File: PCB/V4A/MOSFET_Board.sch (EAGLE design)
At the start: 68 parts, among them IC101 7805T, Q101 IXTK102N65X2, Q102 BC817-16SMD, Q103 SIRC10DP, Q104 SIRC10DP, Q105 BC817-16SMD, Q106 BC807-16SMD, U101 AD620, U102 AD620, U103 LTC1865L, U104 LT1014I, U105 AD420, U106 LP2985-3.1, X201 SMKDSP_1,5/2, X202 SMKDSP_1,5/2

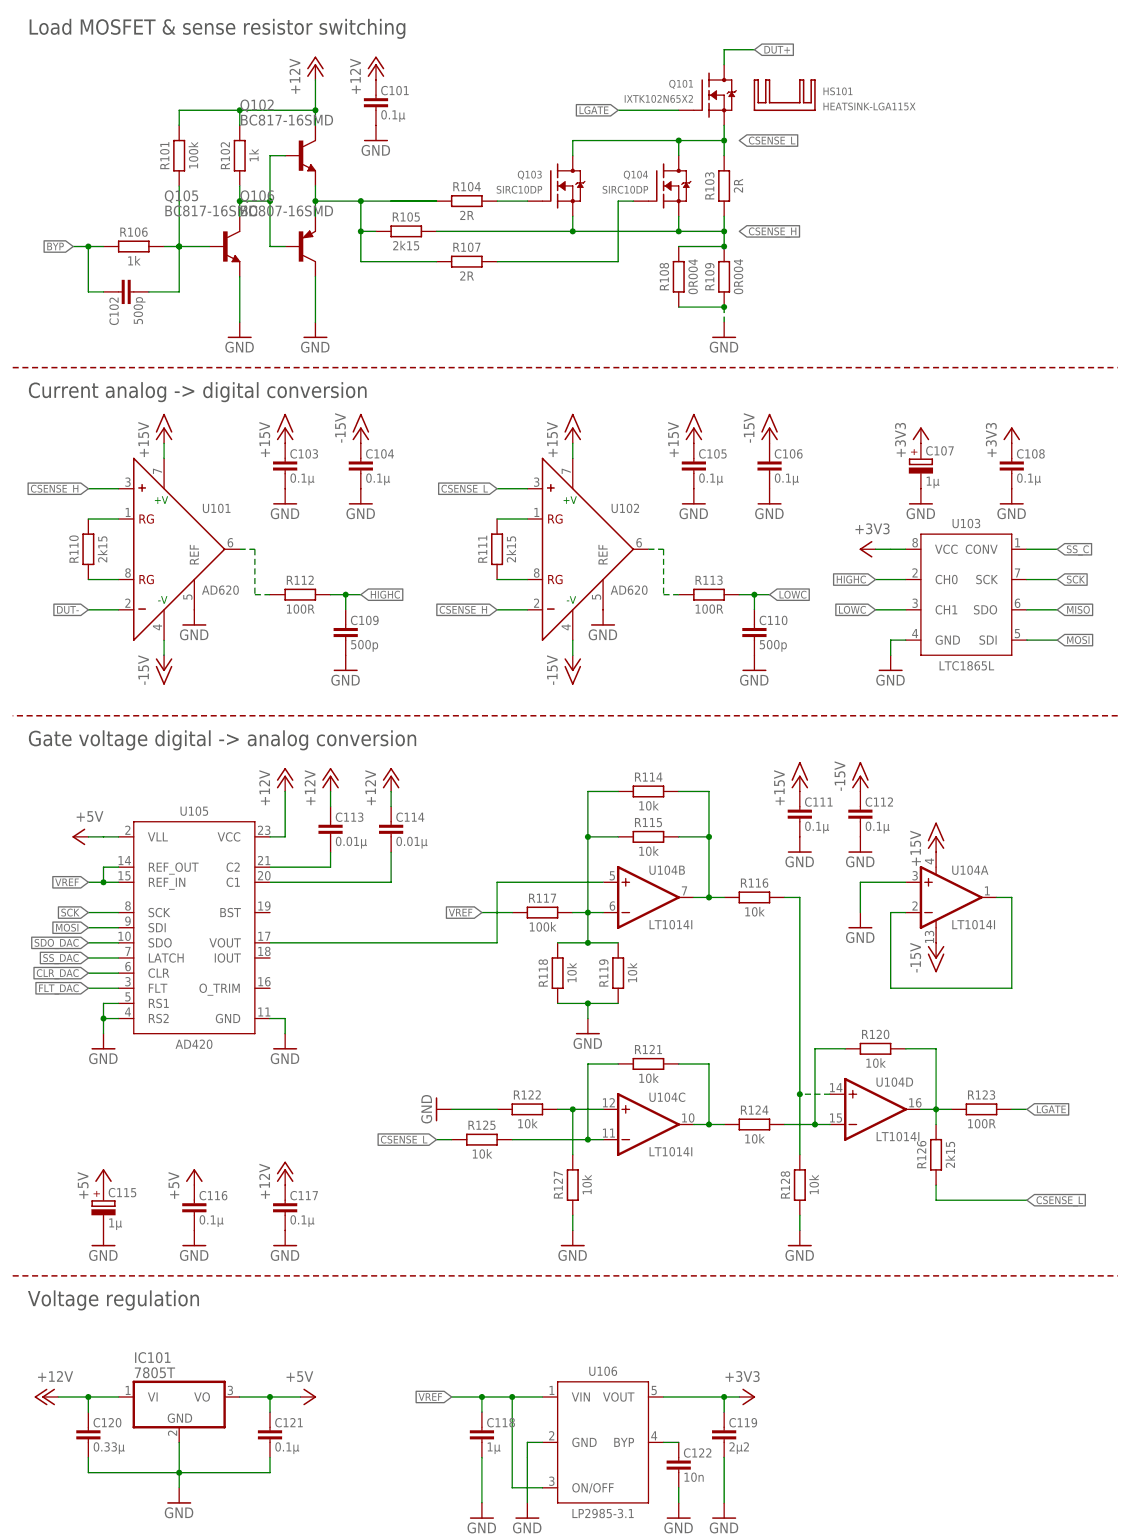
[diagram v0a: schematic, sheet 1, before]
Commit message: Added optoisolation to MOSFET board
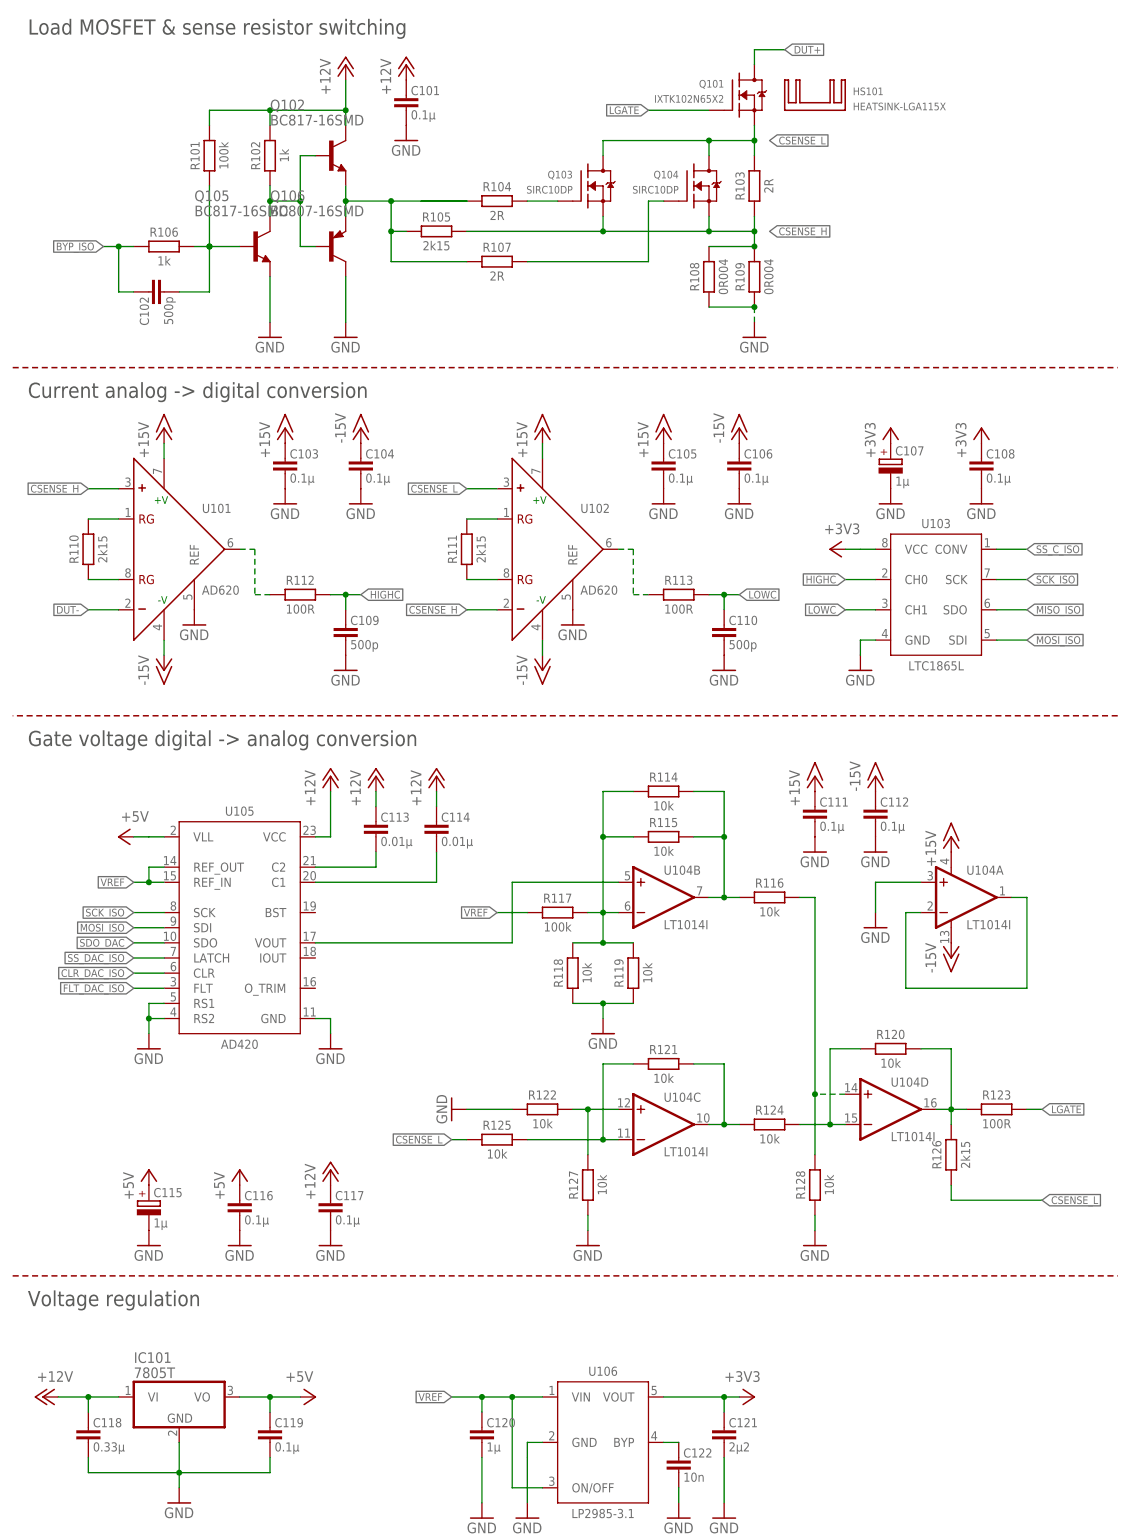
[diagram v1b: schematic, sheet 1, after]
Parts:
- added C201, C203, C209, C211: 0.1µ, passives:C-EU-3216
- added C202, C204, C210, C212: 0.01µ, passives:C-EU-3216
- added C205, C206, C207, C208, C213, C214, C215, C216: 15p, passives:C-EU-1608
- added Q201, Q202, Q203, Q204, Q205, Q206, Q207, Q208: BC807-16SMD, transistor-pnp:BC807-16SMD
- added R201, R202, R203, R204, R205, R206, R207, R208, R209, R210, R211, R212, R213, R214, R215, R216: 350R, passives:R-EU-1608
- added U201, U202, U203, U204: HCPL-063N, ic:HCPL-063N
- C118: value 1µ -> 0.33µ
- C119: value 2µ2 -> 0.1µ
- C120: value 0.33µ -> 1µ
- C121: value 0.1µ -> 2µ2
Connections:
- new net BYP_ISO: C102.1, C213.1, R106.1, R211.1, U203.VO1
- new net CLR_DAC_ISO: C205.1, R203.1, U105.CLR, U201.VO1
- new net FLT_DAC_ISO: Q208.B, U105.FLT
- new net MISO_ISO: Q206.B, U103.SDO
- new net MOSI_ISO: C208.1, R208.1, U103.SDI, U105.SDI, U202.VO2
- new net N$17: Q206.E, R213.1, U204.A1
- new net N$18: Q208.E, R214.1, U204.A2
- new net N$19: Q202.E, R205.1, U202.A1
- new net N$20: Q204.E, R206.1, U202.A2
- new net N$21: Q205.E, R209.1, U203.A1
- new net N$22: Q207.E, R210.1, U203.A2
- new net N$23: JP201.7
- new net N$24: JP201.5
- new net N$26: JP202.1
- new net N$27: JP201.9
- new net N$28: JP201.11
- new net N$29: JP201.13
- new net N$30: JP202.2
- new net N$32: JP201.6
- new net N$33: JP201.8
- new net N$34: JP201.10
- new net N$35: JP201.12
- new net N$36: JP201.14
- new net N$37: JP202.3
- new net N$38: JP202.5
- new net N$39: JP202.7
- new net N$40: JP202.9
- new net N$45: JP202.10
- new net N$46: JP202.8
- new net N$47: JP202.6
- new net N$48: JP202.4
- new net N$76: Q201.E, R201.1, U201.A1
- new net N$77: Q203.E, R202.1, U201.A2
- new net SCK_ISO: C207.1, R207.1, U103.SCK, U105.SCK, U202.VO1
- new net SS_C_ISO: C214.1, R212.1, U103.CONV, U203.VO2
- new net SS_DAC_ISO: C206.1, R204.1, U105.LATCH, U201.VO2
- net +12V: now also C118.1, JP201.3, JP202.11; no longer C120.1
- net +15V: now also JP201.1, JP202.13
- net +3V3: now also C121.1, R207.2, R208.2, R212.2; no longer C119.1
- net +5V: now also C119.1, C201.1, C202.1, C203.1, C204.1, C209.1, C210.1, C211.1, C212.1, R201.2, R202.2, R203.2, R204.2, R205.2, R206.2, R209.2, R210.2, R211.2, R213.2, R214.2, R215.2, R216.2, U201.VCC, U202.VCC, U203.VCC, U204.VCC; no longer C121.1
- net -15V: now also JP201.2, JP202.14
- net BYP: now also Q205.B; no longer C102.1, R106.1
- net CLR_DAC: now also Q201.B; no longer U105.CLR
- net FLT_DAC: now also C216.1, R216.1, U204.VO2; no longer U105.FLT
- net GND: now also C201.2, C202.2, C203.2, C204.2, C205.2, C206.2, C207.2, C208.2, C209.2, C210.2, C211.2, C212.2, C213.2, C214.2, C215.2, C216.2, JP201.4, JP202.12, Q201.C, Q202.C, Q203.C, Q204.C, Q205.C, Q206.C, Q207.C, Q208.C, U201.C1, U201.C2, U201.GND, U202.C1, U202.C2, U202.GND, U203.C1, U203.C2, U203.GND, U204.C1, U204.C2, U204.GND
- net MISO: now also C215.1, R215.1, U204.VO1; no longer U103.SDO
- net MOSI: now also Q204.B; no longer U103.SDI, U105.SDI
- net SCK: now also Q202.B; no longer U103.SCK, U105.SCK
- net SS_C: now also Q207.B; no longer U103.CONV
- net SS_DAC: now also Q203.B; no longer U105.LATCH
- net VREF: now also C120.1; no longer C118.1
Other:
- note added: "Isolation and level shifting"
- moved on the sheet: C101, C102, C105, C106, C107, C108, C110, C111, C112, C113, C114, C115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

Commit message: Changed to single board design
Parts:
- removed C201, C203, C209, C211: 0.1µ, passives:C-EU-3216
- removed C202, C204, C210, C212: 0.01µ, passives:C-EU-3216
- removed C205, C206, C207, C208, C213, C214, C215, C216: 15p, passives:C-EU-1608
- removed JP201, JP202: (no value), pinhead:PINHD-2X7
- removed Q201, Q202, Q203, Q204, Q205, Q206, Q207, Q208: BC807-16SMD, transistor-pnp:BC807-16SMD
- removed R201, R202, R203, R204, R205, R206, R207, R208, R209, R210, R211, R212, R213, R214, R215, R216: 350R, passives:R-EU-1608
- removed U201, U202, U203, U204: HCPL-063N, ic:HCPL-063N
- removed X201, X202: SMKDSP_1,5/2, con-phoenix-smkdsp:SMKDSP_1,5/2
- added C123, C124, C131, C132, C134, C301, C302, C309, C310: 0.1µ, passives:C-EU-3216
- added C125, C126, C127, C128: 100p, passives:C-EU-1608
- added C129, C130: 1µ, passives:CPOL-3216-A
- added C133: 0.33µ, passives:C-EU-3216
- added C135: 1µ, passives:C-EU-3216
- added C136: 10n, passives:C-EU-3216
- added C137: 2µ2, passives:C-EU-3216
- added C303, C304, C311, C312: 0.01µ, passives:C-EU-3216
- added C305, C306, C307, C308, C313, C314, C315, C316: 15p, passives:C-EU-1608
- added D101, D102, D103, D104: BAT54S, diode:BAT54S
- added HS102: HEATSINK-LGA115X, mechanical:HEATSINK-LGA115X
- added JP301, JP302: (no value), pinhead:PINHD-2X7
- added LCD1: LCD-20X4, mechanical:LCD-20X4
- added PS101: RFMM-0505S, modules:RFMM-0505S
- added Q107, Q109: BC817, transistors:BC817
- added Q108, Q110, Q301, Q302, Q303, Q304, Q305, Q306, Q307, Q308: BC807, transistors:BC807
- added Q111, Q112: IXTK102N65X2, transistors:IXTK102N65X2R
- added R129, R130: 100R, passives:R-EU-3216
- added R131, R133, R137, R139: 1k, passives:R-EU-1608
- added R132, R134, R138, R140, R143, R144: 2R, passives:R-EU-3216
- added R135, R136: 100k, passives:R-EU-1608
- added R141, R142, R146, R148: 0R004, passives:R-EU-6332
- added R145, R147, R149, R150, R151, R152: 2k15, passives:R-EU-2012
- added R153, R154, R155, R156: 100R, passives:R-EU-2012
- added R301, R302, R303, R304, R305, R306, R307, R308, R309, R310, R311, R312, R313, R314, R315, R316: 350R, passives:R-EU-1608
- added U$1: ARDUINO-MICRO, breakout:ARDUINO-MICRO
- added U107, U108: AD620, ic:AD620R-8
- added U109, U110: LTC1865L, ic:LTC1865L
- added U111: LP2985-3.1, ic:LP2985-3.1
- added U301, U302, U303, U304: HCPL-063N, ic:HCPL-063N
- added X301, X302, X303, X304: SMKDSP_1,5/2, con-phoenix-smkdsp:SMKDSP_1,5/2
- C102: value 500p -> 0.1µ; device passives:C-EU-1608 -> passives:C-EU-3216
- C105, C106, C108: value 0.1µ -> 0.01µ
- C107: value 1µ -> 0.01µ; device passives:CPOL-3216-A -> passives:C-EU-3216
- C109, C110: value 500p -> 1µ; device passives:C-EU-1608 -> passives:CPOL-3216-A
- C113, C114: value 0.01µ -> 0.1µ
- C115: value 1µ -> 0.1µ; device passives:CPOL-3216-A -> passives:C-EU-3216
- C118: value 0.33µ -> 0.1µ
- C120: value 1µ -> 0.1µ
- C121: value 2µ2 -> 0.1µ
- C122: value 10n -> 0.1µ
- Q101: value IXTK102N65X2 -> SIRC10DP; device transistors:IXTK102N65X2R -> transistors:SIRC10DP
- Q102, Q105: value BC817-16SMD -> SIRC10DP; device transistor-npn:BC817-16SMD -> transistors:SIRC10DP
- Q103, Q104: value SIRC10DP -> BC817; device transistors:SIRC10DP -> transistors:BC817
- Q106: value BC807-16SMD -> SIRC10DP; device transistor-pnp:BC807-16SMD -> transistors:SIRC10DP
- R101, R117: value 100k -> 10k
- R102: value 1k -> 10k
- R103, R104, R107: value 2R -> 10k; device passives:R-EU-3216 -> passives:R-EU-1608
- R105: value 2k15 -> 100k; device passives:R-EU-2012 -> passives:R-EU-1608
- R106: value 1k -> 100k
- R108, R109: value 0R004 -> 10k; device passives:R-EU-6332 -> passives:R-EU-1608
- R110, R111, R126: value 2k15 -> 10k; device passives:R-EU-2012 -> passives:R-EU-1608
- R112, R113: value 100R -> 10k; device passives:R-EU-2012 -> passives:R-EU-1608
- R123: value 100R -> 10k; device passives:R-EU-3216 -> passives:R-EU-1608
- R127, R128: value 10k -> 2k15; device passives:R-EU-1608 -> passives:R-EU-2012
- U101, U102: value AD620 -> AD420; device ic:AD620R-8 -> ic:AD420RW-24
- U103: value LTC1865L -> LT1014I; device ic:LTC1865L -> ic:LT1014ISW
- U105: value AD420 -> AD620; device ic:AD420RW-24 -> ic:AD620R-8
- U106: value LP2985-3.1 -> AD620; device ic:LP2985-3.1 -> ic:AD620R-8
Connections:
- removed net BYP_GATE: Q102.E, Q106.E, R104.1, R105.2, R107.1
- removed net CSENSE_H: Q103.S, Q104.S, R103.1, R105.1, R108.2, R109.2, U101.+, U102.-
- removed net CSENSE_L: Q101.S, Q103.D, Q104.D, R103.2, R125.1, R126.1, U102.+
- removed net HIGHC: C109.1, R112.2, U103.CH0
- removed net LBQ12_G: Q103.G, R104.2
- removed net LBQ13_G: Q104.G, R107.2
- removed net LGATE: Q101.G, R123.2
- removed net LOWC: C110.1, R113.2, U103.CH1
- removed net SDO_DAC: U105.SDO
- new net BPY1G1: Q101.G, R132.2
- new net BYP1: Q109.E, Q110.E, R132.1, R138.1, R147.1
- new net BYP1G2: Q105.G, R138.2
- new net BYP2: Q107.E, Q108.E, R134.1, R140.1, R145.2
- new net BYP2G1: Q102.G, R134.2
- new net BYP2G2: Q106.G, R140.2
- new net CLR_DAC1: U101.CLR
- new net CLR_DAC2: U102.CLR
- new net CONV_C1: U109.CONV
- new net CONV_C2: U110.CONV
- new net CSEN_H1: Q101.S, Q105.S, R141.2, R143.1, R146.2, R147.2, U105.+, U106.-
- new net CSEN_H2: Q102.S, Q106.S, R142.2, R144.1, R145.1, R148.2, U107.+, U108.-
- new net CSEN_L1: Q101.D, Q105.D, Q111.S, R101.1, R127.1, R143.2, U106.+
- new net CSEN_L2: Q102.D, Q106.D, Q112.S, R102.1, R128.1, R144.2, U108.+
- new net DAC_VOUT1: U102.VOUT, U104B.+IN
- new net HIGHC1: C125.1, R153.2, U109.CH0
- new net HIGHC2: C127.1, R155.2, U110.CH0
- new net LATCH_DAC: U101.LATCH, U102.LATCH
- new net LGATE_1: Q111.G, R129.2
- new net LGATE_2: Q112.G, R130.2
- new net LOWC1: C126.1, R154.2, U109.CH1
- new net LOWC2: C128.1, R156.2, U110.CH1
- new net N$15: U103A.-IN, U103A.OUT
- new net N$25: Q103.C, Q107.B, Q108.B, R137.1
- new net N$31: Q103.B, R131.2, R135.1
- new net N$41: C106.2, U102.C2
- new net N$42: C108.2, U102.C1
- new net N$43: R106.2, R108.2, R112.2, R116.1, R117.1, U104B.-IN
- new net N$44: R118.2, R122.1, U104C.OUT
- new net N$49: R102.2, R118.1, U104C.-IN
- new net N$50: R104.2, R110.2, U104C.+IN
- new net N$51: R122.2, R126.1, U104D.-IN
- new net N$52: R126.2, R128.2, R130.1, U104D.OUT
- new net N$53: R120.2, R124.2, U104D.+IN
- new net N$54: R116.2, R117.2, R120.1, U104B.OUT
- new net N$56: D103.C1A2, R155.1, U107.OUT
- new net N$57: D104.C1A2, R156.1, U108.OUT
- new net RG1_L1: R151.2, U107.RG@1
- new net RG1_L2: R152.2, U108.RG@1
- new net RG2_L1: R151.1, U107.RG@2
- new net RG2_L2: R152.1, U108.RG@2
- new net SDO_DAC1: U101.SDO, U102.SDI
- new net SDO_DAC2: U102.SDO
- net +12V: now also C105.1, C106.1, C107.1, C108.1, C115.1, C116.1, C133.1, JP301.3, JP302.11, Q107.C, Q109.C, R135.2, R136.2, R137.2, R139.2, U101.VCC, U102.VCC; no longer C101.1, C117.1, C118.1, JP201.3, JP202.11, Q102.C, R101.2, R102.2, U105.VCC
- net +15V: now also C101.1, C102.1, C117.1, C118.1, C119.1, C120.1, JP301.1, JP302.13, U103A.V+, U105.+V, U106.+V, U107.+V, U108.+V; no longer C103.1, C105.1, C111.1, JP201.1, JP202.13, U101.+V, U102.+V
- net +3V3: now also C129.+, C130.+, C131.1, C132.1, C137.1, D101.C2, D102.C2, D103.C2, D104.C2, R308.2, R313.2, R314.2, U109.VCC, U110.VCC, U111.VOUT; no longer C107.+, C108.1, C121.1, R207.2, R208.2, R212.2, U103.VCC, U106.VOUT
- net +5V: now also C109.+, C110.+, C111.1, C112.1, C134.1, C301.1, C302.1, C303.1, C304.1, C309.1, C310.1, C311.1, C312.1, R301.2, R302.2, R303.2, R304.2, R305.2, R306.2, R307.2, R309.2, R310.2, R311.2, R312.2, R315.2, R316.2, U101.VLL, U102.VLL, U301.VCC, U302.VCC, U303.VCC, U304.VCC; no longer C115.+, C116.1, C119.1, C201.1, C202.1, C203.1, C204.1, C209.1, C210.1, C211.1, C212.1, R201.2, R202.2, R203.2, R204.2, R205.2, R206.2, R209.2, R210.2, R211.2, R213.2, R214.2, R215.2, R216.2, U105.VLL, U201.VCC, U202.VCC, U203.VCC, U204.VCC
- net -15V: now also C103.1, C121.1, C122.1, C123.1, C124.1, JP301.2, JP302.14, U103A.V-, U105.-V, U106.-V, U107.-V, U108.-V; no longer C106.1, C112.1, JP201.2, JP202.14, U101.-V, U102.-V
- net BYP: now also Q302.B; no longer Q205.B
- net BYP_ISO: now also C306.1, R131.1, R133.1, R306.1, U302.VO1; no longer C102.1, C213.1, R106.1, R211.1, U203.VO1
- net CLR_DAC: now also Q301.B; no longer Q201.B
- net CLR_DAC_ISO: now also C305.1, R305.1, U301.VO1; no longer C205.1, R203.1, U105.CLR, U201.VO1
- net DAC_VOUT: now also U101.VOUT, U103B.+IN; no longer U104B.+IN, U105.VOUT
- net DUT+: now also Q111.D, Q112.D, X301-1.KL, X301-2.KL; no longer Q101.D, X201-1.KL, X201-2.KL
- net DUT-: now also U105.-, U107.-; no longer U101.-
- net FLT_DAC: now also C316.1, R316.1, U101.FLT, U102.FLT, U304.VO2; no longer C216.1, R216.1, U204.VO2
- net FLT_DAC_ISO: now also Q308.B; no longer Q208.B, U105.FLT
- net GND: now also C102.2, C109.-, C110.-, C113.2, C114.2, C115.2, C123.2, C124.2, C125.2, C126.2, C127.2, C128.2, C129.-, C130.-, C131.2, C132.2, C133.2, C134.2, C135.2, C136.2, C137.2, C301.2, C302.2, C303.2, C304.2, C305.2, C306.2, C307.2, C308.2, C309.2, C310.2, C311.2, C312.2, C313.2, C314.2, C315.2, C316.2, D101.A1, D102.A1, D103.A1, D104.A1, JP301.4, JP302.12, Q103.E, Q104.E, Q108.C, Q110.C, Q301.C, Q302.C, Q303.C, Q304.C, Q305.C, Q306.C, Q307.C, Q308.C, R103.1, R104.1, R107.1, R110.1, R111.1, R112.1, R123.1, R124.1, R141.1, R142.1, R146.1, R148.1, U101.GND, U101.RS1, U101.RS2, U102.GND, U102.RS1, U102.RS2, U103A.+IN, U105.REF, U106.REF, U107.REF, U108.REF, U109.GND, U110.GND, U111.GND, U301.C1, U301.C2, U301.GND, U302.C1, U302.C2, U302.GND, U303.C1, U303.C2, U303.GND, U304.C1, U304.C2, U304.GND, X302-1.KL, X302-2.KL; no longer C105.2, C106.2, C107.-, C108.2, C109.2, C110.2, C115.-, C201.2, C202.2, C203.2, C204.2, C205.2, C206.2, C207.2, C208.2, C209.2, C210.2, C211.2, C212.2, C213.2, C214.2, C215.2, C216.2, JP201.4, JP202.12, Q105.E, Q106.C, Q201.C, Q202.C, Q203.C, Q204.C, Q205.C, Q206.C, Q207.C, Q208.C, R118.1, R119.1, R122.1, R127.1, R128.1, U101.REF, U102.REF, U103.GND, U105.GND, U105.RS1, U105.RS2, U106.GND, U201.C1, U201.C2, U201.GND, U202.C1, U202.C2, U202.GND, U203.C1, U203.C2, U203.GND, U204.C1, U204.C2, U204.GND, X202-1.KL, X202-2.KL
- net MISO: now also C315.1, R315.1, U109.SDO, U110.SDO, U304.VO1; no longer C215.1, R215.1, U204.VO1
- net MISO_ISO: now also Q307.B; no longer Q206.B, U103.SDO
- net MOSI: now also Q306.B, U101.SDI, U109.SDI, U110.SDI; no longer Q204.B
- net MOSI_ISO: now also C314.1, R314.1, U303.VO2; no longer C208.1, R208.1, U103.SDI, U105.SDI, U202.VO2
- net N$1: now also R103.2, R109.2, U103C.+IN; no longer R122.2, R127.2, U104C.+IN
- net N$10: now also C136.1, U111.BYP; no longer C122.1, U106.BYP
- net N$11: now also R113.2, R119.1, U103B.OUT; no longer R115.2, R116.1, U104B.OUT
- net N$12: now also R105.2, R107.2, R111.2, R113.1, U103B.-IN; no longer R115.1, R117.2, R118.2, R119.2, U104B.-IN
- net N$13: now also R115.2, R121.1, U103C.OUT; no longer R121.2, R124.1, U104C.OUT
- net N$14: now also R101.2, R115.1, U103C.-IN; no longer R121.1, R125.2, U104C.-IN
- net N$16: now also D102.C1A2, R154.1, U106.OUT; no longer R113.1, U102.OUT
- net N$17: now also Q307.E, R311.1, U304.A1; no longer Q206.E, R213.1, U204.A1
- net N$18: now also Q308.E, R312.1, U304.A2; no longer Q208.E, R214.1, U204.A2
- net N$19: now also Q305.E, R309.1, U303.A1; no longer Q202.E, R205.1, U202.A1
- net N$2: now also R121.2, R125.1, U103D.-IN; no longer R120.1, R124.2, U104D.-IN
- net N$20: now also Q306.E, R310.1, U303.A2; no longer Q204.E, R206.1, U202.A2
- net N$21: now also Q302.E, R302.1, U302.A1; no longer Q205.E, R209.1, U203.A1
- net N$22: now also Q304.E, R304.1, U302.A2; no longer Q207.E, R210.1, U203.A2
- net N$23: now also JP301.7; no longer JP201.7
- net N$24: now also JP301.5; no longer JP201.5
- net N$26: now also JP302.1; no longer JP202.1
- net N$27: now also JP301.9; no longer JP201.9
- net N$28: now also JP301.11; no longer JP201.11
- net N$29: now also JP301.13; no longer JP201.13
- net N$3: now also C105.2, U101.C2; no longer C113.2, U105.C2
- net N$30: now also JP302.2; no longer JP202.2
- net N$32: now also JP301.6; no longer JP201.6
- net N$33: now also JP301.8; no longer JP201.8
- net N$34: now also JP301.10; no longer JP201.10
- net N$35: now also JP301.12; no longer JP201.12
- net N$36: now also JP301.14; no longer JP201.14
- net N$37: now also JP302.3; no longer JP202.3
- net N$38: now also JP302.5; no longer JP202.5
- net N$39: now also JP302.7; no longer JP202.7
- net N$4: now also C107.2, U101.C1; no longer C114.2, U105.C1
- net N$40: now also JP302.9; no longer JP202.9
- net N$45: now also JP302.10; no longer JP202.10
- net N$46: now also JP302.8; no longer JP202.8
- net N$47: now also JP302.6; no longer JP202.6
- net N$48: now also JP302.4; no longer JP202.4
- net N$5: now also Q104.C, Q109.B, Q110.B, R139.1; no longer Q102.B, Q105.C, Q106.B, R102.1
- net N$6: now also R125.2, R127.2, R129.1, U103D.OUT; no longer R120.2, R123.1, R126.2, U104D.OUT
- net N$7: now also D101.C1A2, R153.1, U105.OUT; no longer R112.1, U101.OUT
- net N$76: now also Q301.E, R301.1, U301.A1; no longer Q201.E, R201.1, U201.A1
- net N$77: now also Q303.E, R303.1, U301.A2; no longer Q203.E, R202.1, U201.A2
- net N$8: now also Q104.B, R133.2, R136.1; no longer C102.2, Q105.B, R101.1, R106.2
- net N$9: now also R119.2, R123.2, U103D.+IN; no longer R116.2, R128.2, U104D.+IN
- net RG1_L3: now also R149.2, U105.RG@1; no longer R110.2, U101.RG@1
- net RG1_L4: now also R150.2, U106.RG@1; no longer R111.2, U102.RG@1
- net RG2_L3: now also R149.1, U105.RG@2; no longer R110.1, U101.RG@2
- net RG2_L4: now also R150.1, U106.RG@2; no longer R111.1, U102.RG@2
- net SCK: now also Q305.B, U101.SCK, U102.SCK, U109.SCK, U110.SCK; no longer Q202.B
- net SCK_ISO: now also C313.1, R313.1, U303.VO1; no longer C207.1, R207.1, U103.SCK, U105.SCK, U202.VO1
- net SS_C: now also Q304.B; no longer Q207.B
- net SS_C_ISO: now also C308.1, R308.1, U302.VO2; no longer C214.1, R212.1, U103.CONV, U203.VO2
- net SS_DAC: now also Q303.B; no longer Q203.B
- net SS_DAC_ISO: now also C307.1, R307.1, U301.VO2; no longer C206.1, R204.1, U105.LATCH, U201.VO2
- net VREF: now also C135.1, R105.1, R106.1, U101.REF_IN, U101.REF_OUT, U102.REF_IN, U111.ON/OFF, U111.VIN; no longer C120.1, R117.1, U105.REF_IN, U105.REF_OUT, U106.ON/OFF, U106.VIN
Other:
- note added: "Current ADC 1"
- note added: "Load gate drive 1"
- note added: "Load gate drive 2"
- note added: "Load path 1"
- note added: "Load path 2"
- note added: "Range switch 1"
- note added: "Range switch 2"
- note added: "Voltage sense Temperature sense Voltage regulator Connectors"
- note removed: "Current analog -> digital conversion"
- note removed: "Gate voltage digital -> analog conversion"
- note removed: "Load MOSFET & sense resistor switching"
- note removed: "Voltage regulation"

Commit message: PCB layout
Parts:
- removed C133: 0.33µ, passives:C-EU-3216
- removed C134: 0.1µ, passives:C-EU-3216
- removed IC101: 7805T, linear:7805T
- removed JP301, JP302: (no value), pinhead:PINHD-2X7
- removed LCD1: LCD-20X4, mechanical:LCD-20X4
- removed U$1: ARDUINO-MICRO, breakout:ARDUINO-MICRO
- removed X301, X302, X303, X304: SMKDSP_1,5/2, con-phoenix-smkdsp:SMKDSP_1,5/2
- added C1, C11, C220, C3, C6: 1µ, passives:CPOL-3216-A
- added C10: 10µ, passives:CPOL-6032-C
- added C12, C8: 10n, passives:C-EU-3216
- added C13: 22µ, passives:CPOL-6032-C
- added C14, C15: 220µ, rcl:CPOL-EUE3.5-10
- added C16, C18: 0.33µ, passives:C-EU-3216
- added C17, C19: 0.1µ, passives:C-EU-1608
- added C2, C215, C219, C221, C7, C9: 0.1µ, passives:C-EU-3216
- added C218, C4, C5: 500p, passives:C-EU-1608
- added D301, D302: 1N5817-B, diode:1N5817-B
- added IC1, IC2: 7805T, linear:7805T
- added J1: (no value), con-jack:JACK-PLUG1
- added JP1: (no value), pinhead:PINHD-1X16
- added L301, L302: 100µ, passives:L-EUSRN1060
- added MOV201, MOV202, MOV203, MOV204: 180V, passives:MOV-3225
- added R1, R2: 0R01, passives:R-EU-6332
- added R205, R206, R207, R212, R213: 2M, passives:R-EU-3216
- added R214, R215: 2k15, passives:R-EU-2012
- added R216, R3, R4: 100R, passives:R-EU-2012
- added R217: 10k, passives:R-EU-1608
- added U$2, U$3: FAN_MOLEX4PIN, mechanical:FAN_MOLEX4PIN
- added U1, U2: LM50, ic:LM50
- added U205: AD620, ic:AD620R-8
- added U208, U3: LTC1865L, ic:LTC1865L
- added U4: MAX743, ic:MAX743WE
- added X1: GMSTBA4, con-phoenix-762:GMSTBA4
- C101, C102, C103, C104, C111, C112, C113, C114, C115, C116, C117, C118, C119, C120, C121, C122, C123, C124, C131, C132, C301, C302, C309, C310: device passives:C-EU-3216 -> passives:C-EU-1608
- C105, C107, C136: device passives:C-EU-3216 -> passives:C-EU-2012
- C137: value 2µ2 -> 4µ7
- R141, R142, R146, R148: value 0R004 -> 0R01
- R143, R144: value 2R -> 3R3
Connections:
- removed net N$40: JP302.9
- removed net N$46: JP302.8
- removed net N$47: JP302.6
- removed net N$48: JP302.4
- removed net VREF: C135.1, R105.1, R106.1, U101.REF_IN, U101.REF_OUT, U102.REF_IN, U111.ON/OFF, U111.VIN
- new net +5V_I: C310.1, C312.1, PS101.+VO
- new net FAN1_PWM: U$2.PWM
- new net FAN1_SIG: U$2.SIG
- new net FAN2_PWM: U$3.PWM
- new net FAN2_SIG: U$3.SIG
- new net GNDI: C310.2, C312.2, C315.2, C316.2, PS101.-VO, Q301.C, Q302.C, Q303.C, Q304.C, Q305.C, Q306.C, U301.C1, U301.C2, U302.C1, U302.C2, U303.C1, U303.C2, U304.GND
- new net MISO_I: U208.SDO, U3.SDO
- new net MOSI_I: U208.SDI, U3.SDI
- new net RG1_H6: R215.2, U205.RG@1
- new net RG2_H6: R215.1, U205.RG@2
- new net SCK_I: U208.SCK, U3.SCK
- new net SS_TEMP_I: U3.CONV
- new net SS_V_I: U208.CONV
- new net T1_OUT: C1.+, R3.1, U1.VO
- new net T2_OUT: C3.+, R4.1, U2.VO
- new net TEMP1: C4.1, R3.2, U3.CH0
- new net TEMP2: C5.1, R4.2, U3.CH1
- new net VREF1: C135.1, R105.1, U101.REF_IN, U101.REF_OUT, U111.ON/OFF, U111.VIN
- new net VREF2: C10.+, R106.1, U102.REF_IN, U102.REF_OUT, U4.VREF
- new net VSENSE+: MOV201.1, R205.1, X1-1.1
- new net VSENSE-: MOV204.2, U205.-, X1-4.1
- net +12V: now also C16.1, C18.1, IC1.VI, IC2.VI, J1.3, U$2.+12V, U$3.+12V; no longer C133.1, IC101.VI, JP301.3, JP302.11
- net +15V: now also C14.+, C215.1, D301.C, U205.+V, U4.FB+; no longer JP301.1, JP302.13
- net +3V3: now also C220.+, C221.1, C6.+, C7.1, U208.VCC, U3.VCC
- net +5V: now also C13.+, C17.1, C19.1, C2.1, C9.2, IC1.VO, IC2.VO, L302.1, PS101.+VI, U1.+V, U2.+V, U4.AV+, U4.V+, U4.V+@1, U4.V+@2, U4.V+@3; no longer C134.1, C310.1, C312.1, IC101.VO
- net -15V: now also C15.-, C219.1, D302.A, U205.-V, U4.FB-; no longer JP301.2, JP302.14
- net CSEN_H1: now also R1.2
- net CSEN_H2: now also R2.2
- net DUT+: now also X1-2.1; no longer X301-1.KL, X301-2.KL
- net DUT-: now also R1.1, R103.1, R104.1, R141.1, R142.1, R146.1, R148.1, R2.1, X1-3.1
- net GND: now also C1.-, C10.-, C11.-, C12.2, C13.-, C14.-, C15.+, C16.2, C17.2, C18.2, C19.2, C2.2, C215.2, C218.2, C219.2, C220.-, C221.2, C3.-, C4.2, C5.2, C6.-, C7.2, C8.1, C9.1, IC1.GND, IC2.GND, J1.1, L301.2, PS101.-VI, R214.1, R217.1, U$2.GND, U$3.GND, U1.GND, U2.GND, U205.REF, U208.GND, U3.GND, U4.12/15, U4.AGND, U4.GND; no longer C133.2, C134.2, C310.2, C312.2, C315.2, C316.2, IC101.GND, JP301.4, JP302.12, Q301.C, Q302.C, Q303.C, Q304.C, Q305.C, Q306.C, R103.1, R104.1, R141.1, R142.1, R146.1, R148.1, U301.C1, U301.C2, U302.C1, U302.C2, U303.C1, U303.C2, U304.GND, X302-1.KL, X302-2.KL
- net N$23: now also R216.1, U205.OUT; no longer JP301.7
- net N$24: now also R212.1, R213.2; no longer JP301.5
- net N$26: now also R206.2, R212.2; no longer JP302.1
- net N$27: now also R206.1, R207.2; no longer JP301.9
- net N$28: now also MOV201.2, MOV202.1; no longer JP301.11
- net N$29: now also R213.1, R214.2, U205.+; no longer JP301.13
- net N$30: now also C218.1, R216.2, U208.CH0; no longer JP302.2
- net N$32: now also MOV202.2, MOV203.1; no longer JP301.6
- net N$33: now also R205.2, R207.1; no longer JP301.8
- net N$34: now also C12.1, U4.CC-; no longer JP301.10
- net N$35: now also C11.+, U4.SS; no longer JP301.12
- net N$36: now also MOV203.2, MOV204.1; no longer JP301.14
- net N$37: now also C8.2, U4.CC+; no longer JP302.3
- net N$38: now also D301.A, L302.2, U4.LX+; no longer JP302.5
- net N$39: now also D302.C, L301.1, U4.LX-; no longer JP302.7
- net N$45: now also R217.2, U208.CH1; no longer JP302.10
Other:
- note removed: "Connectors to DUT"

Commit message: Added block diagram
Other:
- note added: "+12V"
- note added: "+12VDC"
- note added: "+15V"
- note added: "+15VDC"
- note added: "+3VDC"
- note added: "+5V"
- note added: "+5VDC"
- note added: "-15V"
- note added: "-15VDC"
- note added: "0R002"
- note added: "2R"
- note added: "5VDC<-5VDC"
- note added: "7805"
- note added: "Current ADC 2"
- note added: "DAC"
- note added: "DUT"
- note added: "Gate Drive"
- note added: "Gate Drive 1"
- note added: "Gate drive 2"
- note added: "I/O"
- note added: "LDO"
- note added: "MAX743"
- note added: "MOSFET"
- note added: "Optocouplers"
- note added: "Range Switch"
- note added: "TODO: block diagram"
- note added: "Vout"
- note added: "Vref"
- note removed: "Load gate drive 1"
- note removed: "Load gate drive 2"
